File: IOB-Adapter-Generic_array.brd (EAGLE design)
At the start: 106.7 x 104.1 mm, 53 parts

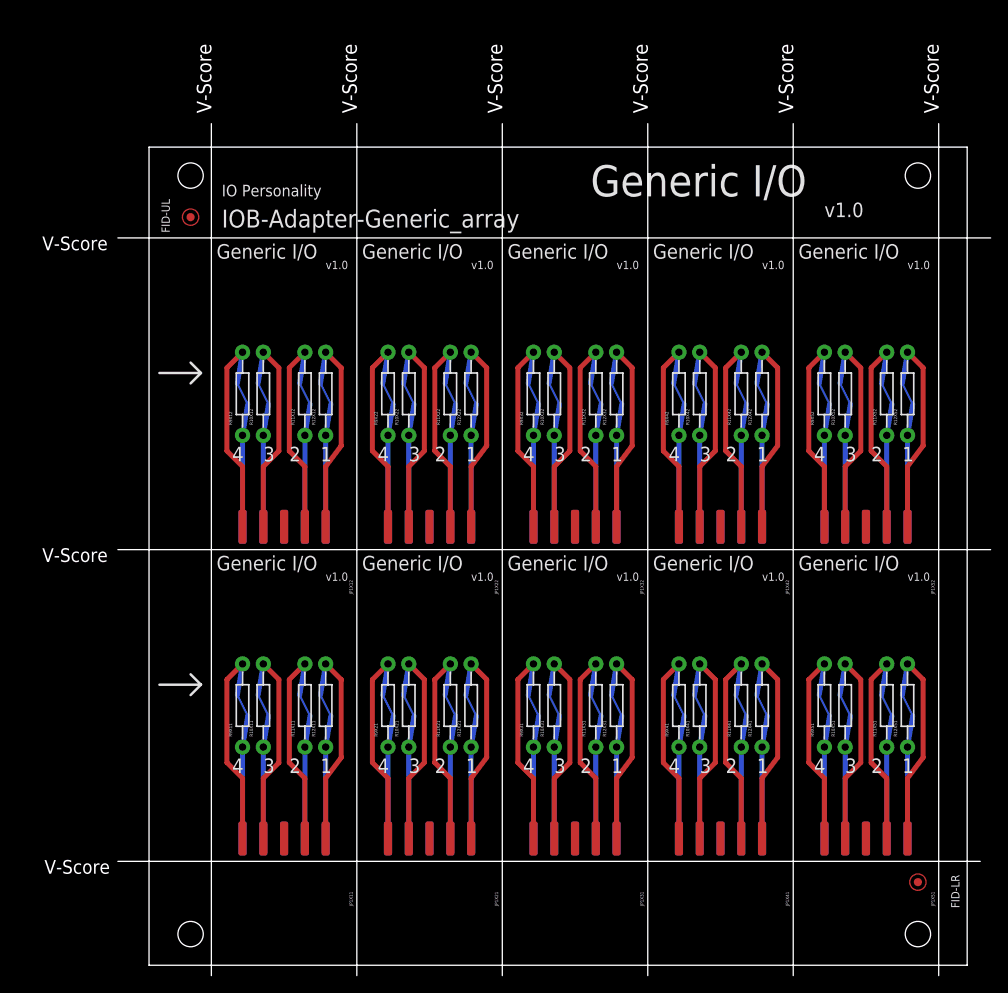
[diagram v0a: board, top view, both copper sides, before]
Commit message: change from edge to PTH mount
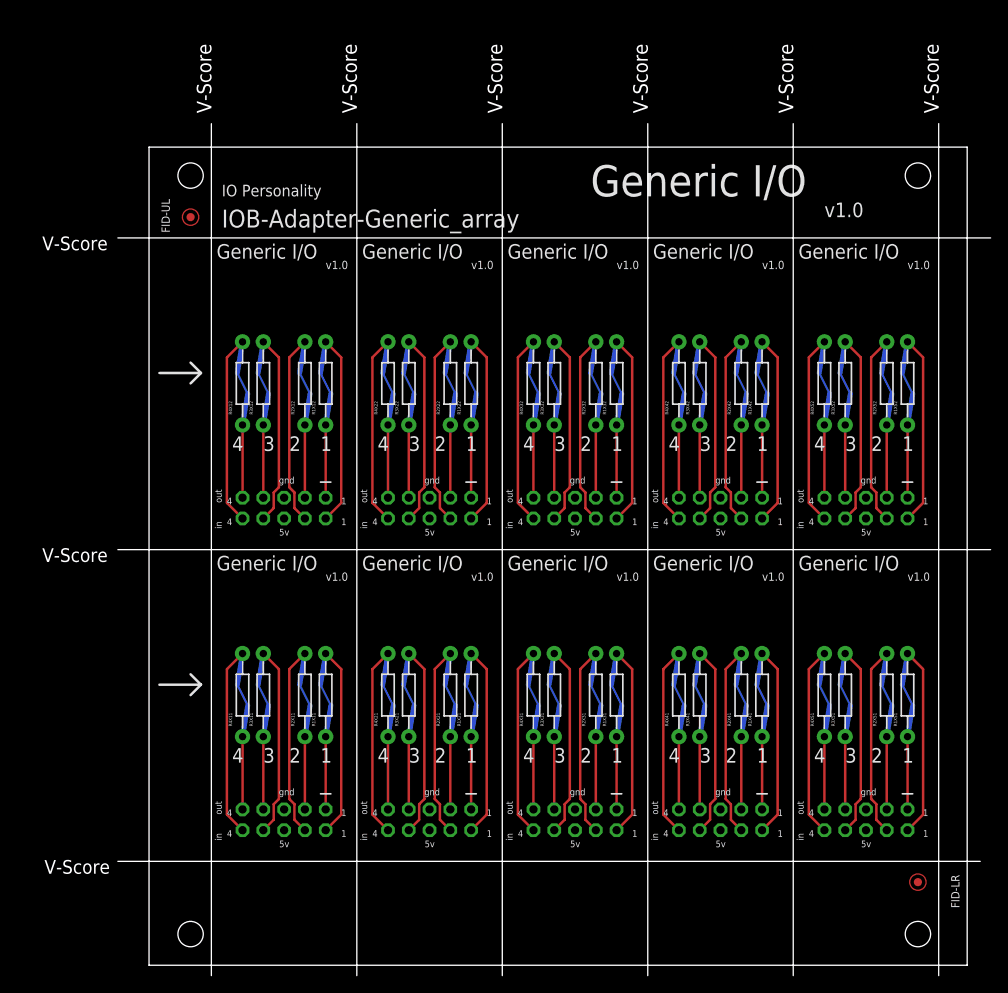
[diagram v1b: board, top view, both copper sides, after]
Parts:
- removed R10X11, R10X12, R10X21, R10X22, R10X31, R10X32, R10X41, R10X42, R10X51, R10X52, R11X11, R11X12, R11X21, R11X22, R11X31, R11X32, R11X41, R11X42, R11X51, R11X52, R12X11, R12X12, R12X21, R12X22, R12X31, R12X32, R12X41, R12X42, R12X51, R12X52, R9X11, R9X12, R9X21, R9X22, R9X31, R9X32, R9X41, R9X42, R9X51, R9X52: NOSTUFF, SPCoast:CUT-R
- added R1X11, R1X12, R1X21, R1X22, R1X31, R1X32, R1X41, R1X42, R1X51, R1X52, R2X11, R2X12, R2X21, R2X22, R2X31, R2X32, R2X41, R2X42, R2X51, R2X52, R3X11, R3X12, R3X21, R3X22, R3X31, R3X32, R3X41, R3X42, R3X51, R3X52, R4X11, R4X12, R4X21, R4X22, R4X31, R4X32, R4X41, R4X42, R4X51, R4X52: NOSTUFF, SPCoast:CUT-R
- JP1X11, JP1X12, JP1X21, JP1X22, JP1X31, JP1X32, JP1X41, JP1X42, JP1X51, JP1X52: value CONNECTOR-M05X2EDGE -> CONNECTOR-M05X2; device SPCoast:2X5-EDGE -> SPCoast:IOB-V3-MODULE
- moved JP1X12 5.08 mm to (16.5, 55.9), flipped to the bottom, turned to 270 degrees
- moved JP1X22 5.08 mm to (34.3, 55.9), flipped to the bottom, turned to 270 degrees
- moved JP1X32 5.08 mm to (52.1, 55.9), flipped to the bottom, turned to 270 degrees
- moved JP1X42 5.08 mm to (69.8, 55.9), flipped to the bottom, turned to 270 degrees
- moved JP1X52 5.08 mm to (87.6, 55.9), flipped to the bottom, turned to 270 degrees
- moved JP1X11 5.08 mm to (16.5, 17.8), flipped to the bottom, turned to 270 degrees
- moved JP1X21 5.08 mm to (34.3, 17.8), flipped to the bottom, turned to 270 degrees
- moved JP1X31 5.08 mm to (52.1, 17.8), flipped to the bottom, turned to 270 degrees
- moved JP1X41 5.08 mm to (69.8, 17.8), flipped to the bottom, turned to 270 degrees
- moved JP1X51 5.08 mm to (87.6, 17.8), flipped to the bottom, turned to 270 degrees
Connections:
- net N$1X11: now also R1X11.P2; no longer R9X11.P2
- net N$1X12: now also R1X12.P2; no longer R9X12.P2
- net N$1X21: now also R1X21.P2; no longer R9X21.P2
- net N$1X22: now also R1X22.P2; no longer R9X22.P2
- net N$1X31: now also R1X31.P2; no longer R9X31.P2
- net N$1X32: now also R1X32.P2; no longer R9X32.P2
- net N$1X41: now also R1X41.P2; no longer R9X41.P2
- net N$1X42: now also R1X42.P2; no longer R9X42.P2
- net N$1X51: now also R1X51.P2; no longer R9X51.P2
- net N$1X52: now also R1X52.P2; no longer R9X52.P2
- net N$2X11: now also R2X11.P2; no longer R10X11.P2
- net N$2X12: now also R2X12.P2; no longer R10X12.P2
- net N$2X21: now also R2X21.P2; no longer R10X21.P2
- net N$2X22: now also R2X22.P2; no longer R10X22.P2
- net N$2X31: now also R2X31.P2; no longer R10X31.P2
- net N$2X32: now also R2X32.P2; no longer R10X32.P2
- net N$2X41: now also R2X41.P2; no longer R10X41.P2
- net N$2X42: now also R2X42.P2; no longer R10X42.P2
- net N$2X51: now also R2X51.P2; no longer R10X51.P2
- net N$2X52: now also R2X52.P2; no longer R10X52.P2
- net N$3X11: now also R3X11.P2; no longer R11X11.P2
- net N$3X12: now also R3X12.P2; no longer R11X12.P2
- net N$3X21: now also R3X21.P2; no longer R11X21.P2
- net N$3X22: now also R3X22.P2; no longer R11X22.P2
- net N$3X31: now also R3X31.P2; no longer R11X31.P2
- net N$3X32: now also R3X32.P2; no longer R11X32.P2
- net N$3X41: now also R3X41.P2; no longer R11X41.P2
- net N$3X42: now also R3X42.P2; no longer R11X42.P2
- net N$3X51: now also R3X51.P2; no longer R11X51.P2
- net N$3X52: now also R3X52.P2; no longer R11X52.P2
- net N$4X11: now also R4X11.P2; no longer R12X11.P2
- net N$4X12: now also R4X12.P2; no longer R12X12.P2
- net N$4X21: now also R4X21.P2; no longer R12X21.P2
- net N$4X22: now also R4X22.P2; no longer R12X22.P2
- net N$4X31: now also R4X31.P2; no longer R12X31.P2
- net N$4X32: now also R4X32.P2; no longer R12X32.P2
- net N$4X41: now also R4X41.P2; no longer R12X41.P2
- net N$4X42: now also R4X42.P2; no longer R12X42.P2
- net N$4X51: now also R4X51.P2; no longer R12X51.P2
- net N$4X52: now also R4X52.P2; no longer R12X52.P2
- net P1X11: now also R1X11.P1; no longer R9X11.P1
- net P1X12: now also R1X12.P1; no longer R9X12.P1
- net P1X21: now also R1X21.P1; no longer R9X21.P1
- net P1X22: now also R1X22.P1; no longer R9X22.P1
- net P1X31: now also R1X31.P1; no longer R9X31.P1
- net P1X32: now also R1X32.P1; no longer R9X32.P1
- net P1X41: now also R1X41.P1; no longer R9X41.P1
- net P1X42: now also R1X42.P1; no longer R9X42.P1
- net P1X51: now also R1X51.P1; no longer R9X51.P1
- net P1X52: now also R1X52.P1; no longer R9X52.P1
- net P2X11: now also R2X11.P1; no longer R10X11.P1
- net P2X12: now also R2X12.P1; no longer R10X12.P1
- net P2X21: now also R2X21.P1; no longer R10X21.P1
- net P2X22: now also R2X22.P1; no longer R10X22.P1
- net P2X31: now also R2X31.P1; no longer R10X31.P1
- net P2X32: now also R2X32.P1; no longer R10X32.P1
- net P2X41: now also R2X41.P1; no longer R10X41.P1
- net P2X42: now also R2X42.P1; no longer R10X42.P1
- net P2X51: now also R2X51.P1; no longer R10X51.P1
- net P2X52: now also R2X52.P1; no longer R10X52.P1
- net P3X11: now also R3X11.P1; no longer R11X11.P1
- net P3X12: now also R3X12.P1; no longer R11X12.P1
- net P3X21: now also R3X21.P1; no longer R11X21.P1
- net P3X22: now also R3X22.P1; no longer R11X22.P1
- net P3X31: now also R3X31.P1; no longer R11X31.P1
- net P3X32: now also R3X32.P1; no longer R11X32.P1
- net P3X41: now also R3X41.P1; no longer R11X41.P1
- net P3X42: now also R3X42.P1; no longer R11X42.P1
- net P3X51: now also R3X51.P1; no longer R11X51.P1
- net P3X52: now also R3X52.P1; no longer R11X52.P1
- net P4X11: now also R4X11.P1; no longer R12X11.P1
- net P4X12: now also R4X12.P1; no longer R12X12.P1
- net P4X21: now also R4X21.P1; no longer R12X21.P1
- net P4X22: now also R4X22.P1; no longer R12X22.P1
- net P4X31: now also R4X31.P1; no longer R12X31.P1
- net P4X32: now also R4X32.P1; no longer R12X32.P1
- net P4X41: now also R4X41.P1; no longer R12X41.P1
- net P4X42: now also R4X42.P1; no longer R12X42.P1
- net P4X51: now also R4X51.P1; no longer R12X51.P1
- net P4X52: now also R4X52.P1; no longer R12X52.P1
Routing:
- net N$4X51: track 11.2 -> 8.89 mm
- net N$4X41: track 11.2 -> 8.89 mm
- net N$4X31: track 11.2 -> 8.89 mm
- net N$4X21: track 11.2 -> 8.89 mm
- net N$4X11: track 11.2 -> 8.89 mm
- net N$3X51: track 11.2 -> 8.89 mm
- net N$3X41: track 11.2 -> 8.89 mm
- net N$3X31: track 11.2 -> 8.89 mm
- net N$3X21: track 11.2 -> 8.89 mm
- net N$3X11: track 11.2 -> 8.89 mm
- net N$2X51: track 11.2 -> 8.89 mm
- net N$2X41: track 11.2 -> 8.89 mm
- net N$2X31: track 11.2 -> 8.89 mm
- net N$2X21: track 11.2 -> 8.89 mm
- net N$2X11: track 11.2 -> 8.89 mm
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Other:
- board text added: "GENERIC I/O"
- board text added: "R1"
- board text added: "R2"
- board text added: "R3"
- board text added: "R4"
- board text removed: "I/O Driver Board"
- board text removed: "R10"
- board text removed: "R11"
- board text removed: "R12"
- board text removed: "R9"
